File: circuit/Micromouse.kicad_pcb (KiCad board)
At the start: 2 copper layers, 78 x 100 mm, 84 parts, among them CN1 Battery, CN2 Battery, J1 DBG_CN, J3 TEST_1P, J5 TEST_1P, J6 Conn_01x04, J7 Conn_02x03_Odd_Even, J8 Conn_02x03_Odd_Even, Q1 IRLML6402, Q2 IRLML6344, Q3 ST-1KL3A, Q5 ST-1KL3A, Q7 ST-1KL3A, Q9 ST-1KL3A, SW0 SW_Push, SW1 SW_Push, SW1 SW_SPDT, SW2 SW_Push, U1 NJM7805S, U2 TB6612FNG, U3 STM32F405RGTx, U4 ADP7182AUJZ-3.3, U5 AD8397, U6 AD8397, U7 ICM-20602-module

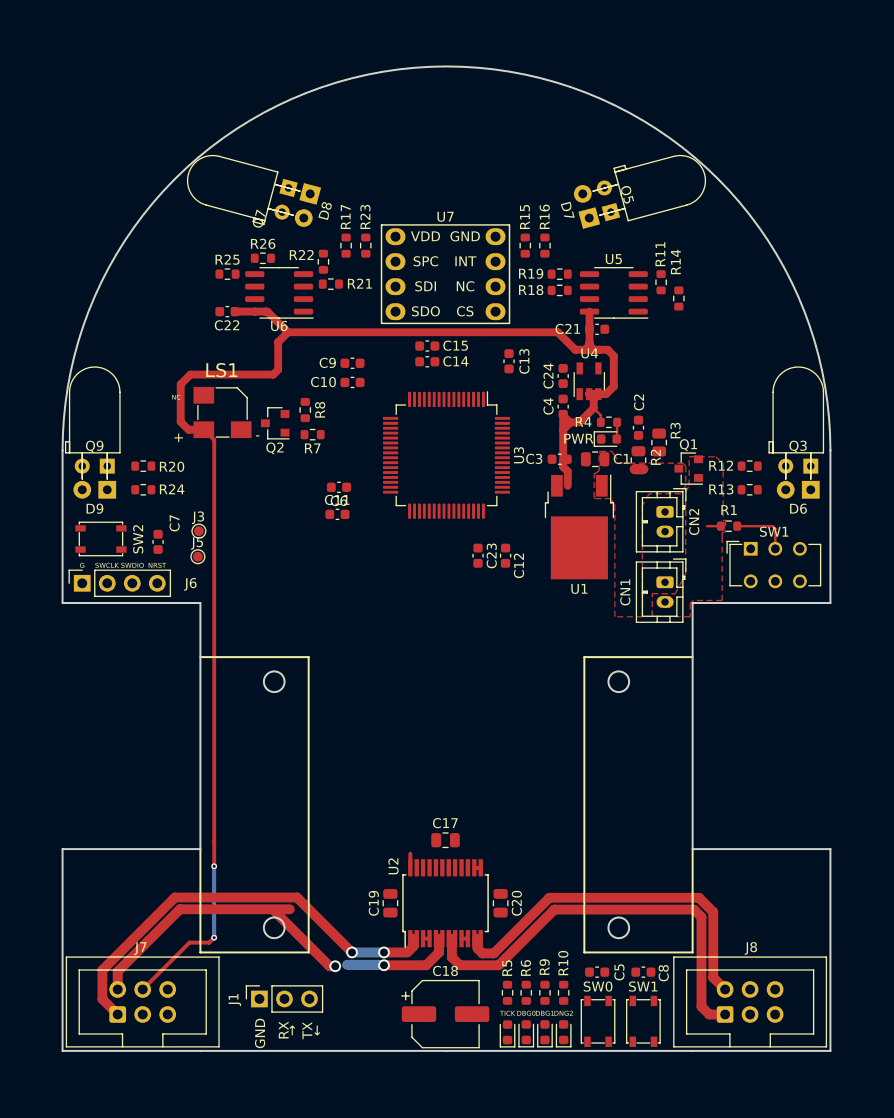
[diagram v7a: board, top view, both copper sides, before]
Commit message: 残すはGNDビアとGND分離・・・
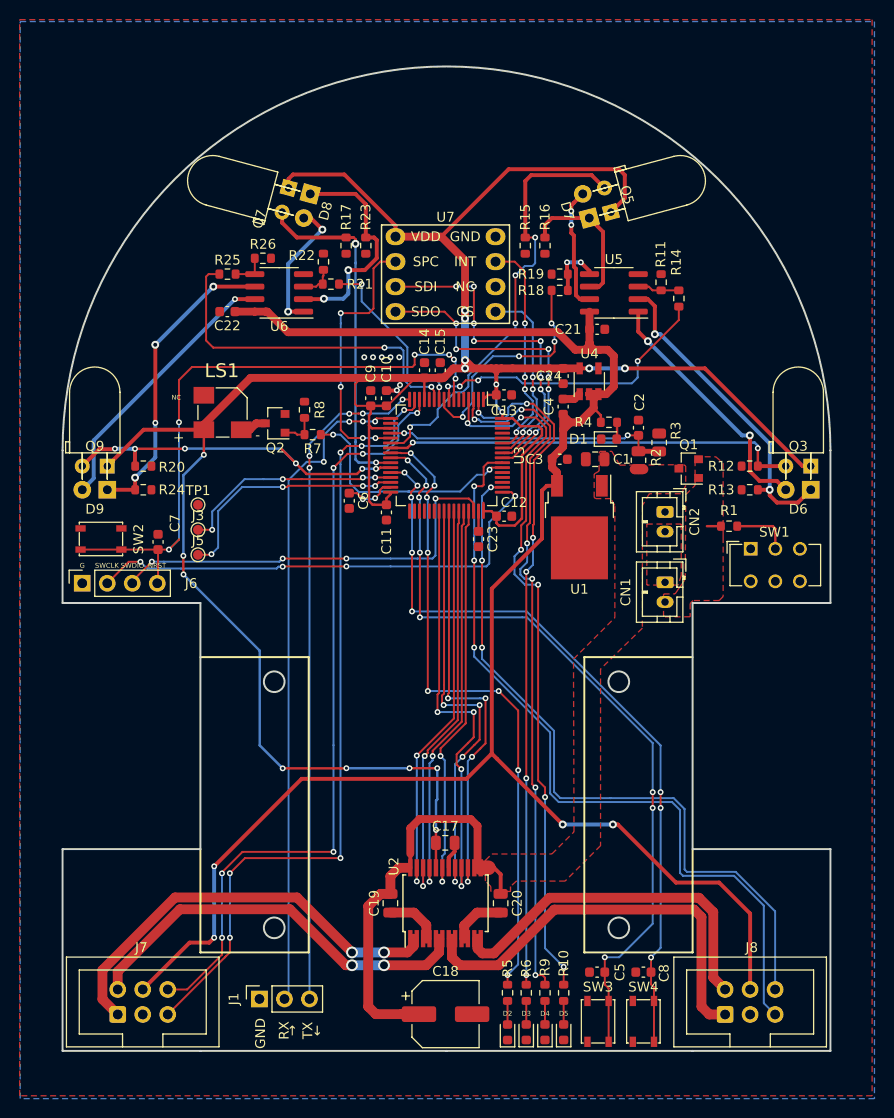
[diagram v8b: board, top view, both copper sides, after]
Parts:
- added TP1: TestPoint, TestPoint:TestPoint_Pad_D1.0mm, F.Cu at (119.5, 87.2)
- moved C11 4.98 mm to (138.6, 88.0), turned to 270 degrees
- moved C12 4.02 mm to (150.6, 88.4), turned to 0 degrees
- moved C9 4.00 mm to (137.0, 76.4), turned to 90 degrees
- moved C10 3.80 mm to (138.6, 76.4), turned to 90 degrees
- moved C13 3.45 mm to (150.5, 76.1), turned to 0 degrees
- moved C15 2.79 mm to (144.1, 73.6), turned to 270 degrees
- moved C6 1.72 mm to (134.8, 86.8), turned to 270 degrees
- moved C23 1.69 mm to (148.0, 90.7)
- moved C14 0.91 mm to (142.5, 73.6), turned to 270 degrees
- moved C17 0.27 mm to (144.6, 121.6)
- moved J5 0.19 mm to (119.5, 92.3)
- moved J3 0.16 mm to (119.5, 89.8)
- moved R8 0.08 mm to (130.3, 77.6)
- renumbered PWR to D1, TICK to D2, DBG0 to D3, DBG1 to D4, DNG2 to D5, SW0 to SW3, SW1 to SW4
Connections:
- LS1 pad 1: +5V -> +3V3
- U3 pad 14: /ENC_R_A -> /ENC_L_A
- U3 pad 15: /ENC_R_B -> /ENC_L_B
- U3 pad 22: /WALL_SEN0 -> /WALL_SEN1
- U3 pad 23: /WALL_SEN1 -> /WALL_SEN0
- U3 pad 25: Net-(U3-Pad25) -> /SW0
- U3 pad 50: /ENC_L_A -> /ENC_R_A
- U3 pad 55: /ENC_L_B -> /ENC_R_B
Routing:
- net +3V3: track 0.00 -> 266.7 mm, vias 0 -> 16
- net /ENC_L_B: track 0.00 -> 81.4 mm, vias 0 -> 6
- net /SW0: track 0.00 -> 81.2 mm, vias 0 -> 8
- net /ENC_R_B: track 0.00 -> 81.1 mm, vias 0 -> 3
- net /ENC_L_A: track 0.00 -> 79.9 mm, vias 0 -> 6
- net /SW1: track 0.00 -> 78.0 mm, vias 0 -> 8
- net /ENC_R_A: track 0.00 -> 74.6 mm, vias 0 -> 3
- net /DBG_LED2: track 0.00 -> 72.1 mm, vias 0 -> 6
- net /DBG_LED1: track 0.00 -> 71.1 mm, vias 0 -> 6
- net /DBG_LED0: track 0.00 -> 69.3 mm, vias 0 -> 6
- net /DBG_TX: track 0.00 -> 68.4 mm, vias 0 -> 5
- net /DBG_RX: track 0.00 -> 67.8 mm, vias 0 -> 5
- net /TICK_LED: track 0.00 -> 65.9 mm, vias 0 -> 8
- net /NRST: track 0.00 -> 65.6 mm, vias 0 -> 6
- net /SWCLK: track 0.00 -> 49.6 mm, vias 0 -> 4
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- added copper zone on B.Cu, net GND
- added copper zone on F.Cu, net GND
- added copper zone on F.Cu, net Net-(CN1-Pad1)
